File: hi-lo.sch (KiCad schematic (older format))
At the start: 25 parts, among them U31 TC4427, U32 TC4427, U33 TC4427

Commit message: from Ola and Jared (#71)
* Update

* removed fp-info-cache from git

* Gerbers

* moved connector

* Mostly Ola's e-mailed copy, plus some of my own fixes to his almost done revision. I also did some house cleaning, with boundary edges, removed most DRC and ERC errors, etc.

* added Fiducial's
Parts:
- C17, C78: footprint Capacitor_SMD:C_0603_1608Metric_Pad1.05x0.95mm_HandSolder -> Capacitor_SMD:C_0603_1608Metric
- R104, R105, R106, R107, R108, R109, R112, R113, R114, R115, R116, R117, R120, R121, R122, R123, R124, R125, R57, R59: footprint Resistor_SMD:R_0603_1608Metric_Pad1.05x0.95mm_HandSolder -> Resistor_SMD:R_0603_1608Metric
- U31, U32, U33: footprint Package_SO:SO-8_3.9x4.9mm_P1.27mm -> modules:DFN-8-1EP_6x5mm_P1.27mm_EP4x2mm
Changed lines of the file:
@@
 Sheet 3 7
 Title "microRusEfi"
-Date "2019-04-12"
-Rev "0.5.5"
+Date "2019-07-01"
+Rev "R0.2"
 Comp "rusEFI.com"
 Comment1 ""
@@
 F 0 "R125" V 7730 8300 40  0000 C CNN
 F 1 "100" V 7657 8301 40  0000 C CNN
-F 2 "Resistor_SMD:R_0603_1608Metric_Pad1.05x0.95mm_HandSolder" V 980 3050 60  0001 C CNN
+F 2 "Resistor_SMD:R_0603_1608Metric" V 980 3050 60  0001 C CNN
 F 3 "" H 7650 8300 60  0001 C CNN
 	1    7650 8300
@@
 F 0 "R124" V 7730 7700 40  0000 C CNN
 F 1 "100" V 7657 7701 40  0000 C CNN
-F 2 "Resistor_SMD:R_0603_1608Metric_Pad1.05x0.95mm_HandSolder" V 980 3050 60  0001 C CNN
+F 2 "Resistor_SMD:R_0603_1608Metric" V 980 3050 60  0001 C CNN
 F 3 "" H 7650 7700 60  0001 C CNN
 	1    7650 7700
@@
 F 0 "U33" H 6500 8200 60  0000 C CNN
 F 1 "TC4427" H 6650 7700 50  0000 C CNN
-F 2 "Package_SO:SO-8_3.9x4.9mm_P1.27mm" H 6500 7950 60  0001 C CNN
+F 2 "modules:DFN-8-1EP_6x5mm_P1.27mm_EP4x2mm" H 6500 7950 60  0001 C CNN
 F 3 "" H 6500 7950 60  0000 C CNN
 F 4 "579-TC4427EOA" H 0   0   50  0001 C CNN "Part #"
@@
 F 0 "R116" V 5975 8000 40  0000 C CNN
 F 1 "1k" V 5907 8001 40  0000 C CNN
-F 2 "Resistor_SMD:R_0603_1608Metric_Pad1.05x0.95mm_HandSolder" V -770 5150 60  0001 C CNN
+F 2 "Resistor_SMD:R_0603_1608Metric" V -770 5150 60  0001 C CNN
 F 3 "" H 5900 8000 60  0001 C CNN
 	1    5900 8000
@@
 F 0 "R108" V 5475 7900 40  0000 C CNN
 F 1 "20R" V 5407 7901 40  0000 C CNN
-F 2 "Resistor_SMD:R_0603_1608Metric_Pad1.05x0.95mm_HandSolder" V -1270 5050 60  0001 C CNN
+F 2 "Resistor_SMD:R_0603_1608Metric" V -1270 5050 60  0001 C CNN
 F 3 "" H 5400 7900 60  0001 C CNN
 	1    5400 7900
@@
 F 0 "R117" V 5975 8200 40  0000 C CNN
 F 1 "1k" V 5907 8201 40  0000 C CNN
-F 2 "Resistor_SMD:R_0603_1608Metric_Pad1.05x0.95mm_HandSolder" V -770 5350 60  0001 C CNN
+F 2 "Resistor_SMD:R_0603_1608Metric" V -770 5350 60  0001 C CNN
 F 3 "" H 5900 8200 60  0001 C CNN
 	1    5900 8200
@@
 F 0 "R109" V 5475 8100 40  0000 C CNN
 F 1 "20R" V 5407 8101 40  0000 C CNN
-F 2 "Resistor_SMD:R_0603_1608Metric_Pad1.05x0.95mm_HandSolder" V -1270 5250 60  0001 C CNN
+F 2 "Resistor_SMD:R_0603_1608Metric" V -1270 5250 60  0001 C CNN
 F 3 "" H 5400 8100 60  0001 C CNN
 	1    5400 8100
@@
 F 0 "R123" V 7680 7100 40  0000 C CNN
 F 1 "100" V 7607 7101 40  0000 C CNN
-F 2 "Resistor_SMD:R_0603_1608Metric_Pad1.05x0.95mm_HandSolder" V 930 1850 60  0001 C CNN
+F 2 "Resistor_SMD:R_0603_1608Metric" V 930 1850 60  0001 C CNN
 F 3 "" H 7600 7100 60  0001 C CNN
 	1    7600 7100
@@
 F 0 "R122" V 7680 6500 40  0000 C CNN
 F 1 "100" V 7607 6501 40  0000 C CNN
-F 2 "Resistor_SMD:R_0603_1608Metric_Pad1.05x0.95mm_HandSolder" V 930 1850 60  0001 C CNN
+F 2 "Resistor_SMD:R_0603_1608Metric" V 930 1850 60  0001 C CNN
 F 3 "" H 7600 6500 60  0001 C CNN
 	1    7600 6500
@@
 F 0 "U32" H 6450 7000 60  0000 C CNN
 F 1 "TC4427" H 6600 6500 50  0000 C CNN
-F 2 "Package_SO:SO-8_3.9x4.9mm_P1.27mm" H 6450 6750 60  0001 C CNN
+F 2 "modules:DFN-8-1EP_6x5mm_P1.27mm_EP4x2mm" H 6450 6750 60  0001 C CNN
 F 3 "" H 6450 6750 60  0000 C CNN
 F 4 "579-TC4427EOA" H 0   0   50  0001 C CNN "Part #"
@@
 F 0 "R114" V 5925 6800 40  0000 C CNN
 F 1 "1k" V 5857 6801 40  0000 C CNN
-F 2 "Resistor_SMD:R_0603_1608Metric_Pad1.05x0.95mm_HandSolder" V -820 3950 60  0001 C CNN
+F 2 "Resistor_SMD:R_0603_1608Metric" V -820 3950 60  0001 C CNN
 F 3 "" H 5850 6800 60  0001 C CNN
 	1    5850 6800
@@
 F 0 "R106" V 5425 6700 40  0000 C CNN
 F 1 "20R" V 5357 6701 40  0000 C CNN
-F 2 "Resistor_SMD:R_0603_1608Metric_Pad1.05x0.95mm_HandSolder" V -1320 3850 60  0001 C CNN
+F 2 "Resistor_SMD:R_0603_1608Metric" V -1320 3850 60  0001 C CNN
 F 3 "" H 5350 6700 60  0001 C CNN
 	1    5350 6700
@@
 F 0 "R115" V 5925 7000 40  0000 C CNN
 F 1 "1k" V 5857 7001 40  0000 C CNN
-F 2 "Resistor_SMD:R_0603_1608Metric_Pad1.05x0.95mm_HandSolder" V -820 4150 60  0001 C CNN
+F 2 "Resistor_SMD:R_0603_1608Metric" V -820 4150 60  0001 C CNN
 F 3 "" H 5850 7000 60  0001 C CNN
 	1    5850 7000
@@
 F 0 "R107" V 5425 6900 40  0000 C CNN
 F 1 "20R" V 5357 6901 40  0000 C CNN
-F 2 "Resistor_SMD:R_0603_1608Metric_Pad1.05x0.95mm_HandSolder" V -1320 4050 60  0001 C CNN
+F 2 "Resistor_SMD:R_0603_1608Metric" V -1320 4050 60  0001 C CNN
 F 3 "" H 5350 6900 60  0001 C CNN
 	1    5350 6900
@@
 F 0 "C78" V 4250 6850 40  0000 L CNN
 F 1 "10nF" V 4250 6550 40  0000 L CNN
-F 2 "Capacitor_SMD:C_0603_1608Metric_Pad1.05x0.95mm_HandSolder" V -2120 1850 60  0001 C CNN
+F 2 "Capacitor_SMD:C_0603_1608Metric" V -2120 1850 60  0001 C CNN
 F 3 "" H 4200 6800 60  0001 C CNN
 	1    4200 6800
@@
 F 0 "R121" V 7630 5750 40  0000 C CNN
 F 1 "100" V 7557 5751 40  0000 C CNN
-F 2 "Resistor_SMD:R_0603_1608Metric_Pad1.05x0.95mm_HandSolder" V 880 500 60  0001 C CNN
+F 2 "Resistor_SMD:R_0603_1608Metric" V 880 500 60  0001 C CNN
 F 3 "" H 7550 5750 60  0001 C CNN
 	1    7550 5750
@@
 F 0 "R120" V 7630 5150 40  0000 C CNN
 F 1 "100" V 7557 5151 40  0000 C CNN
-F 2 "Resistor_SMD:R_0603_1608Metric_Pad1.05x0.95mm_HandSolder" V 880 500 60  0001 C CNN
+F 2 "Resistor_SMD:R_0603_1608Metric" V 880 500 60  0001 C CNN
 F 3 "" H 7550 5150 60  0001 C CNN
 	1    7550 5150
@@
 F 0 "U31" H 6400 5650 60  0000 C CNN
 F 1 "TC4427" H 6550 5150 50  0000 C CNN
-F 2 "Package_SO:SO-8_3.9x4.9mm_P1.27mm" H 6400 5400 60  0001 C CNN
+F 2 "modules:DFN-8-1EP_6x5mm_P1.27mm_EP4x2mm" H 6400 5400 60  0001 C CNN
 F 3 "" H 6400 5400 60  0000 C CNN
 F 4 "579-TC4427EOA" H 0   0   50  0001 C CNN "Part #"
@@
 F 0 "R112" V 5875 5450 40  0000 C CNN
 F 1 "1k" V 5807 5451 40  0000 C CNN
-F 2 "Resistor_SMD:R_0603_1608Metric_Pad1.05x0.95mm_HandSolder" V -870 2600 60  0001 C CNN
+F 2 "Resistor_SMD:R_0603_1608Metric" V -870 2600 60  0001 C CNN
 F 3 "" H 5800 5450 60  0001 C CNN
 	1    5800 5450
@@
 F 0 "R104" V 5375 5350 40  0000 C CNN
 F 1 "20R" V 5307 5351 40  0000 C CNN
-F 2 "Resistor_SMD:R_0603_1608Metric_Pad1.05x0.95mm_HandSolder" V -1370 2500 60  0001 C CNN
+F 2 "Resistor_SMD:R_0603_1608Metric" V -1370 2500 60  0001 C CNN
 F 3 "" H 5300 5350 60  0001 C CNN
 	1    5300 5350
@@
 F 0 "R113" V 5875 5650 40  0000 C CNN
 F 1 "1k" V 5807 5651 40  0000 C CNN
-F 2 "Resistor_SMD:R_0603_1608Metric_Pad1.05x0.95mm_HandSolder" V -870 2800 60  0001 C CNN
+F 2 "Resistor_SMD:R_0603_1608Metric" V -870 2800 60  0001 C CNN
 F 3 "" H 5800 5650 60  0001 C CNN
 	1    5800 5650
@@
 F 0 "R105" V 5375 5550 40  0000 C CNN
 F 1 "20R" V 5307 5551 40  0000 C CNN
-F 2 "Resistor_SMD:R_0603_1608Metric_Pad1.05x0.95mm_HandSolder" V -1370 2700 60  0001 C CNN
+F 2 "Resistor_SMD:R_0603_1608Metric" V -1370 2700 60  0001 C CNN
 F 3 "" H 5300 5550 60  0001 C CNN
 	1    5300 5550
@@
 F 0 "C17" V 4050 5150 40  0000 L CNN
 F 1 "10nF" V 4050 4850 40  0000 L CNN
-F 2 "Capacitor_SMD:C_0603_1608Metric_Pad1.05x0.95mm_HandSolder" V -2320 150 60  0001 C CNN
+F 2 "Capacitor_SMD:C_0603_1608Metric" V -2320 150 60  0001 C CNN
 F 3 "" H 4000 5100 60  0001 C CNN
 	1    4000 5100
@@
 F 0 "R59" V 3175 5100 40  0000 C CNN
 F 1 "0R" V 3107 5101 40  0000 C CNN
-F 2 "Resistor_SMD:R_0603_1608Metric_Pad1.05x0.95mm_HandSolder" V -3570 2250 60  0001 C CNN
+F 2 "Resistor_SMD:R_0603_1608Metric" V -3570 2250 60  0001 C CNN
 F 3 "" H 3100 5100 60  0001 C CNN
 	1    3100 5100
@@
 F 0 "R57" V 3175 4800 40  0000 C CNN
 F 1 "DNP" V 3107 4801 40  0000 C CNN
-F 2 "Resistor_SMD:R_0603_1608Metric_Pad1.05x0.95mm_HandSolder" V -3570 1950 60  0001 C CNN
+F 2 "Resistor_SMD:R_0603_1608Metric" V -3570 1950 60  0001 C CNN
 F 3 "" H 3100 4800 60  0001 C CNN
 	1    3100 4800

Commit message: Updated logo symbol and footprint, BOM is 99% entered in KC schematic now.
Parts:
- C17, C78: Manufacturer (none) -> KEMET; Part # (none) -> C0603C103K1RACTU; VEND (none) -> DIGI; VEND# (none) -> 399-3189-1-ND
- R104, R105, R106, R107, R108, R109: Manufacturer (none) -> StackPole; Part # (none) -> RMCF0603JT20R0; VEND (none) -> DIGI; VEND# (none) -> RMCF0603JT20R0CT-ND
- R112, R113, R114, R115, R116, R117: Manufacturer (none) -> StackPole; Part # (none) -> RMCF0603JJ1K00; VEND (none) -> DIGI; VEND# (none) -> RMCF0603JJ1K00CT-ND
- R120, R121, R122, R123, R124, R125: Manufacturer (none) -> StackPole; Part # (none) -> RMCF0603FT100R; VEND (none) -> DIGI; VEND# (none) -> RMCF0603FT100RCT-ND
- R57: Manufacturer (none) -> DNP; Part # (none) -> DNP; VEND (none) -> DIGI; VEND# (none) -> DNP
- R59: Manufacturer (none) -> StackPole; Part # (none) -> RMCF0603ZT0R00; VEND (none) -> DIGI; VEND# (none) -> RMCF0603ZT0R00CT-ND
- U31, U32, U33: Manufacturer (none) -> MicroChip; Part # 579-TC4427EOA -> TC4427EOA; VEND (none) -> DIGI; VEND# 579-TC4427EOA -> TC4427EOA-ND
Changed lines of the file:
@@
 F 2 "Resistor_SMD:R_0603_1608Metric" V 980 3050 60  0001 C CNN
 F 3 "" H 7650 8300 60  0001 C CNN
+F 4 "RMCF0603FT100R" H 0   0   50  0001 C CNN "Part #"
+F 5 "DIGI" H 0   0   50  0001 C CNN "VEND"
+F 6 "RMCF0603FT100RCT-ND" H 0   0   50  0001 C CNN "VEND#"
+F 7 "StackPole" H 0   0   50  0001 C CNN "Manufacturer"
 	1    7650 8300
 	0    1    1    0
@@
 F 2 "Resistor_SMD:R_0603_1608Metric" V 980 3050 60  0001 C CNN
 F 3 "" H 7650 7700 60  0001 C CNN
+F 4 "RMCF0603FT100R" H 0   0   50  0001 C CNN "Part #"
+F 5 "DIGI" H 0   0   50  0001 C CNN "VEND"
+F 6 "RMCF0603FT100RCT-ND" H 0   0   50  0001 C CNN "VEND#"
+F 7 "StackPole" H 0   0   50  0001 C CNN "Manufacturer"
 	1    7650 7700
 	0    1    -1   0
@@
 F 2 "modules:DFN-8-1EP_6x5mm_P1.27mm_EP4x2mm" H 6500 7950 60  0001 C CNN
 F 3 "" H 6500 7950 60  0000 C CNN
-F 4 "579-TC4427EOA" H 0   0   50  0001 C CNN "Part #"
-F 5 "579-TC4427EOA" H 0   0   50  0001 C CNN "VEND#"
+F 4 "TC4427EOA" H 0   0   50  0001 C CNN "Part #"
+F 5 "TC4427EOA-ND" H 0   0   50  0001 C CNN "VEND#"
+F 6 "DIGI" H 0   0   50  0001 C CNN "VEND"
+F 7 "MicroChip" H 0   0   50  0001 C CNN "Manufacturer"
 	1    6500 7950
 	1    0    0    -1
@@
 F 2 "Resistor_SMD:R_0603_1608Metric" V -770 5150 60  0001 C CNN
 F 3 "" H 5900 8000 60  0001 C CNN
+F 4 "RMCF0603JJ1K00" H 0   0   50  0001 C CNN "Part #"
+F 5 "DIGI" H 0   0   50  0001 C CNN "VEND"
+F 6 "RMCF0603JJ1K00CT-ND" H 0   0   50  0001 C CNN "VEND#"
+F 7 "StackPole" H 0   0   50  0001 C CNN "Manufacturer"
 	1    5900 8000
 	0    1    -1   0
@@
 F 2 "Resistor_SMD:R_0603_1608Metric" V -1270 5050 60  0001 C CNN
 F 3 "" H 5400 7900 60  0001 C CNN
+F 4 "RMCF0603JT20R0" H 0   0   50  0001 C CNN "Part #"
+F 5 "DIGI" H 0   0   50  0001 C CNN "VEND"
+F 6 "RMCF0603JT20R0CT-ND" H 0   0   50  0001 C CNN "VEND#"
+F 7 "StackPole" H 0   0   50  0001 C CNN "Manufacturer"
 	1    5400 7900
 	0    1    -1   0
@@
 F 2 "Resistor_SMD:R_0603_1608Metric" V -770 5350 60  0001 C CNN
 F 3 "" H 5900 8200 60  0001 C CNN
+F 4 "RMCF0603JJ1K00" H 0   0   50  0001 C CNN "Part #"
+F 5 "DIGI" H 0   0   50  0001 C CNN "VEND"
+F 6 "RMCF0603JJ1K00CT-ND" H 0   0   50  0001 C CNN "VEND#"
+F 7 "StackPole" H 0   0   50  0001 C CNN "Manufacturer"
 	1    5900 8200
 	0    1    -1   0
@@
 F 2 "Resistor_SMD:R_0603_1608Metric" V -1270 5250 60  0001 C CNN
 F 3 "" H 5400 8100 60  0001 C CNN
+F 4 "RMCF0603JT20R0" H 0   0   50  0001 C CNN "Part #"
+F 5 "DIGI" H 0   0   50  0001 C CNN "VEND"
+F 6 "RMCF0603JT20R0CT-ND" H 0   0   50  0001 C CNN "VEND#"
+F 7 "StackPole" H 0   0   50  0001 C CNN "Manufacturer"
 	1    5400 8100
 	0    1    -1   0
@@
 F 2 "Resistor_SMD:R_0603_1608Metric" V 930 1850 60  0001 C CNN
 F 3 "" H 7600 7100 60  0001 C CNN
+F 4 "RMCF0603FT100R" H 0   0   50  0001 C CNN "Part #"
+F 5 "DIGI" H 0   0   50  0001 C CNN "VEND"
+F 6 "RMCF0603FT100RCT-ND" H 0   0   50  0001 C CNN "VEND#"
+F 7 "StackPole" H 0   0   50  0001 C CNN "Manufacturer"
 	1    7600 7100
 	0    1    1    0
@@
 F 2 "Resistor_SMD:R_0603_1608Metric" V 930 1850 60  0001 C CNN
 F 3 "" H 7600 6500 60  0001 C CNN
+F 4 "RMCF0603FT100R" H 0   0   50  0001 C CNN "Part #"
+F 5 "DIGI" H 0   0   50  0001 C CNN "VEND"
+F 6 "RMCF0603FT100RCT-ND" H 0   0   50  0001 C CNN "VEND#"
+F 7 "StackPole" H 0   0   50  0001 C CNN "Manufacturer"
 	1    7600 6500
 	0    1    -1   0
@@
 F 2 "modules:DFN-8-1EP_6x5mm_P1.27mm_EP4x2mm" H 6450 6750 60  0001 C CNN
 F 3 "" H 6450 6750 60  0000 C CNN
-F 4 "579-TC4427EOA" H 0   0   50  0001 C CNN "Part #"
-F 5 "579-TC4427EOA" H 0   0   50  0001 C CNN "VEND#"
+F 4 "TC4427EOA" H 0   0   50  0001 C CNN "Part #"
+F 5 "TC4427EOA-ND" H 0   0   50  0001 C CNN "VEND#"
+F 6 "DIGI" H 0   0   50  0001 C CNN "VEND"
+F 7 "MicroChip" H 0   0   50  0001 C CNN "Manufacturer"
 	1    6450 6750
 	1    0    0    -1
@@
 F 2 "Resistor_SMD:R_0603_1608Metric" V -820 3950 60  0001 C CNN
 F 3 "" H 5850 6800 60  0001 C CNN
+F 4 "RMCF0603JJ1K00" H 0   0   50  0001 C CNN "Part #"
+F 5 "DIGI" H 0   0   50  0001 C CNN "VEND"
+F 6 "RMCF0603JJ1K00CT-ND" H 0   0   50  0001 C CNN "VEND#"
+F 7 "StackPole" H 0   0   50  0001 C CNN "Manufacturer"
 	1    5850 6800
 	0    1    -1   0
@@
 F 2 "Resistor_SMD:R_0603_1608Metric" V -1320 3850 60  0001 C CNN
 F 3 "" H 5350 6700 60  0001 C CNN
+F 4 "RMCF0603JT20R0" H 0   0   50  0001 C CNN "Part #"
+F 5 "DIGI" H 0   0   50  0001 C CNN "VEND"
+F 6 "RMCF0603JT20R0CT-ND" H 0   0   50  0001 C CNN "VEND#"
+F 7 "StackPole" H 0   0   50  0001 C CNN "Manufacturer"
 	1    5350 6700
 	0    1    -1   0
@@
 F 2 "Resistor_SMD:R_0603_1608Metric" V -820 4150 60  0001 C CNN
 F 3 "" H 5850 7000 60  0001 C CNN
+F 4 "RMCF0603JJ1K00" H 0   0   50  0001 C CNN "Part #"
+F 5 "DIGI" H 0   0   50  0001 C CNN "VEND"
+F 6 "RMCF0603JJ1K00CT-ND" H 0   0   50  0001 C CNN "VEND#"
+F 7 "StackPole" H 0   0   50  0001 C CNN "Manufacturer"
 	1    5850 7000
 	0    1    -1   0
@@
 F 2 "Resistor_SMD:R_0603_1608Metric" V -1320 4050 60  0001 C CNN
 F 3 "" H 5350 6900 60  0001 C CNN
+F 4 "RMCF0603JT20R0" H 0   0   50  0001 C CNN "Part #"
+F 5 "DIGI" H 0   0   50  0001 C CNN "VEND"
+F 6 "RMCF0603JT20R0CT-ND" H 0   0   50  0001 C CNN "VEND#"
+F 7 "StackPole" H 0   0   50  0001 C CNN "Manufacturer"
 	1    5350 6900
 	0    1    -1   0
@@
 F 2 "Capacitor_SMD:C_0603_1608Metric" V -2120 1850 60  0001 C CNN
 F 3 "" H 4200 6800 60  0001 C CNN
+F 4 "C0603C103K1RACTU" H 0   0   50  0001 C CNN "Part #"
+F 5 "DIGI" H 0   0   50  0001 C CNN "VEND"
+F 6 "399-3189-1-ND" H 0   0   50  0001 C CNN "VEND#"
+F 7 "KEMET" H 0   0   50  0001 C CNN "Manufacturer"
 	1    4200 6800
 	0    1    -1   0
@@
 F 2 "Resistor_SMD:R_0603_1608Metric" V 880 500 60  0001 C CNN
 F 3 "" H 7550 5750 60  0001 C CNN
+F 4 "RMCF0603FT100R" H 0   0   50  0001 C CNN "Part #"
+F 5 "DIGI" H 0   0   50  0001 C CNN "VEND"
+F 6 "RMCF0603FT100RCT-ND" H 0   0   50  0001 C CNN "VEND#"
+F 7 "StackPole" H 0   0   50  0001 C CNN "Manufacturer"
 	1    7550 5750
 	0    1    1    0
@@
 F 2 "Resistor_SMD:R_0603_1608Metric" V 880 500 60  0001 C CNN
 F 3 "" H 7550 5150 60  0001 C CNN
+F 4 "RMCF0603FT100R" H 0   0   50  0001 C CNN "Part #"
+F 5 "DIGI" H 0   0   50  0001 C CNN "VEND"
+F 6 "RMCF0603FT100RCT-ND" H 0   0   50  0001 C CNN "VEND#"
+F 7 "StackPole" H 0   0   50  0001 C CNN "Manufacturer"
 	1    7550 5150
 	0    1    -1   0
@@
 F 2 "modules:DFN-8-1EP_6x5mm_P1.27mm_EP4x2mm" H 6400 5400 60  0001 C CNN
 F 3 "" H 6400 5400 60  0000 C CNN
-F 4 "579-TC4427EOA" H 0   0   50  0001 C CNN "Part #"
-F 5 "579-TC4427EOA" H 0   0   50  0001 C CNN "VEND#"
+F 4 "TC4427EOA" H 0   0   50  0001 C CNN "Part #"
+F 5 "TC4427EOA-ND" H 0   0   50  0001 C CNN "VEND#"
+F 6 "DIGI" H 0   0   50  0001 C CNN "VEND"
+F 7 "MicroChip" H 0   0   50  0001 C CNN "Manufacturer"
 	1    6400 5400
 	1    0    0    -1
@@
 F 2 "Resistor_SMD:R_0603_1608Metric" V -870 2600 60  0001 C CNN
 F 3 "" H 5800 5450 60  0001 C CNN
+F 4 "RMCF0603JJ1K00" H 0   0   50  0001 C CNN "Part #"
+F 5 "DIGI" H 0   0   50  0001 C CNN "VEND"
+F 6 "RMCF0603JJ1K00CT-ND" H 0   0   50  0001 C CNN "VEND#"
+F 7 "StackPole" H 0   0   50  0001 C CNN "Manufacturer"
 	1    5800 5450
 	0    1    -1   0
@@
 F 2 "Resistor_SMD:R_0603_1608Metric" V -1370 2500 60  0001 C CNN
 F 3 "" H 5300 5350 60  0001 C CNN
+F 4 "RMCF0603JT20R0" H 0   0   50  0001 C CNN "Part #"
+F 5 "DIGI" H 0   0   50  0001 C CNN "VEND"
+F 6 "RMCF0603JT20R0CT-ND" H 0   0   50  0001 C CNN "VEND#"
+F 7 "StackPole" H 0   0   50  0001 C CNN "Manufacturer"
 	1    5300 5350
 	0    1    -1   0
@@
 F 2 "Resistor_SMD:R_0603_1608Metric" V -870 2800 60  0001 C CNN
 F 3 "" H 5800 5650 60  0001 C CNN
+F 4 "RMCF0603JJ1K00" H 0   0   50  0001 C CNN "Part #"
+F 5 "DIGI" H 0   0   50  0001 C CNN "VEND"
+F 6 "RMCF0603JJ1K00CT-ND" H 0   0   50  0001 C CNN "VEND#"
+F 7 "StackPole" H 0   0   50  0001 C CNN "Manufacturer"
 	1    5800 5650
 	0    1    -1   0
@@
 F 2 "Resistor_SMD:R_0603_1608Metric" V -1370 2700 60  0001 C CNN
 F 3 "" H 5300 5550 60  0001 C CNN
+F 4 "RMCF0603JT20R0" H 0   0   50  0001 C CNN "Part #"
+F 5 "DIGI" H 0   0   50  0001 C CNN "VEND"
+F 6 "RMCF0603JT20R0CT-ND" H 0   0   50  0001 C CNN "VEND#"
+F 7 "StackPole" H 0   0   50  0001 C CNN "Manufacturer"
 	1    5300 5550
 	0    1    -1   0
@@
 F 2 "Capacitor_SMD:C_0603_1608Metric" V -2320 150 60  0001 C CNN
 F 3 "" H 4000 5100 60  0001 C CNN
+F 4 "C0603C103K1RACTU" H 0   0   50  0001 C CNN "Part #"
+F 5 "DIGI" H 0   0   50  0001 C CNN "VEND"
+F 6 "399-3189-1-ND" H 0   0   50  0001 C CNN "VEND#"
+F 7 "KEMET" H 0   0   50  0001 C CNN "Manufacturer"
 	1    4000 5100
 	-1   0    0    -1
@@
 F 2 "Resistor_SMD:R_0603_1608Metric" V -3570 2250 60  0001 C CNN
 F 3 "" H 3100 5100 60  0001 C CNN
+F 4 "RMCF0603ZT0R00" H 0   0   50  0001 C CNN "Part #"
+F 5 "DIGI" H 0   0   50  0001 C CNN "VEND"
+F 6 "RMCF0603ZT0R00CT-ND" H 0   0   50  0001 C CNN "VEND#"
+F 7 "StackPole" H 0   0   50  0001 C CNN "Manufacturer"
 	1    3100 5100
 	1    0    0    1
@@
 F 2 "Resistor_SMD:R_0603_1608Metric" V -3570 1950 60  0001 C CNN
 F 3 "" H 3100 4800 60  0001 C CNN
+F 4 "DNP" H 0   0   50  0001 C CNN "Part #"
+F 5 "DIGI" H 0   0   50  0001 C CNN "VEND"
+F 6 "DNP" H 0   0   50  0001 C CNN "VEND#"
+F 7 "DNP" H 0   0   50  0001 C CNN "Manufacturer"
 	1    3100 4800
 	1    0    0    1

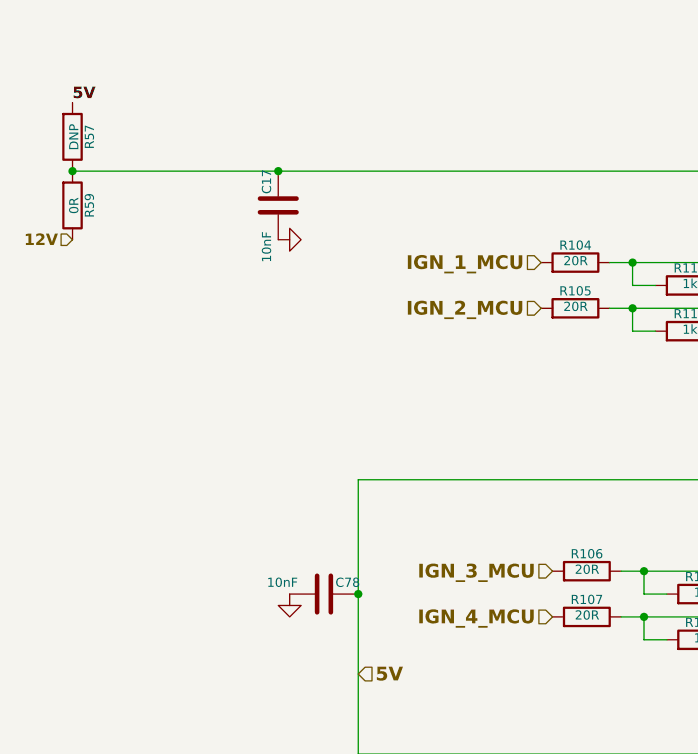
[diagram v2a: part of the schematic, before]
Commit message: sync (#98)
* Added silk screen mark, minor schematic formatting.
https://github.com/rusefi/hw_microRusEfi/issues/89

* Changed SWD connector to reflect validated brain board.
https://github.com/rusefi/hw_microRusEfi/issues/88

* Changed R26 into push button SW1 BOM is still TBD
https://github.com/rusefi/hw_microRusEfi/issues/86

* coil1 silk was corrected to coil2
https://github.com/rusefi/hw_microRusEfi/issues/90

* Updated BOM
https://github.com/rusefi/hw_microRusEfi/issues/94
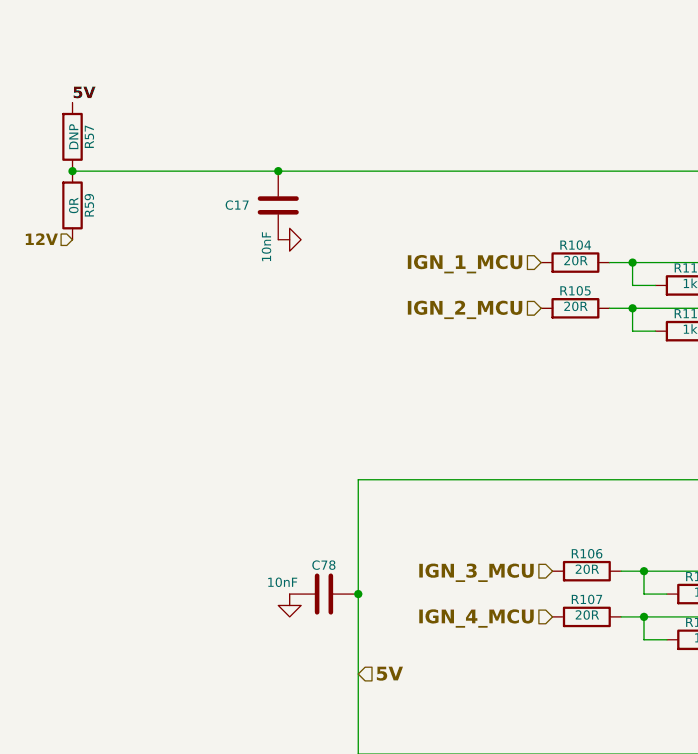
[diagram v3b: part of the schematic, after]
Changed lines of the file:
@@
 U 1 1 5D15752C
 P 4200 6800
-F 0 "C78" V 4250 6850 40  0000 L CNN
+F 0 "C78" V 4325 6800 40  0000 C CNN
 F 1 "10nF" V 4250 6550 40  0000 L CNN
 F 2 "Capacitor_SMD:C_0603_1608Metric" V -2120 1850 60  0001 C CNN
@@
 U 1 1 5E89211D
 P 4000 5100
-F 0 "C17" V 4050 5150 40  0000 L CNN
+F 0 "C17" H 4125 5100 40  0000 L CNN
 F 1 "10nF" V 4050 4850 40  0000 L CNN
 F 2 "Capacitor_SMD:C_0603_1608Metric" V -2320 150 60  0001 C CNN

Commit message: getting closer to 0.3
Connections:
- net HS1 renamed Ign3
- net HS1_MCU renamed Ign3_MCU
- net HS2 renamed Ign4
- net HS2_MCU renamed Ign4_MCU
- net IGN_1 renamed GP5
- net IGN_1_MCU renamed GP5_MCU
- net IGN_2 renamed GP6
- net IGN_2_MCU renamed GP6_MCU
- net IGN_3 renamed Ign1
- net IGN_3_MCU renamed Ign1_MCU
- net IGN_4 renamed Ign2
- net IGN_4_MCU renamed Ign2_MCU
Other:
- note added: "6 channel high / low side driver"
- note removed: "8 channel high / low side driver"
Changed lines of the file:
@@
 $EndDescr
 Text Notes 6250 3300 0    160  ~ 32
-8 channel high / low side driver
+6 channel high / low side driver
 NoConn ~ 6150 7800
 NoConn ~ 6850 7800
@@
 	6850 4950 6850 5450
 Text HLabel 7700 5150 2    60   Input ~ 12
-IGN_1
+GP5
 Text HLabel 7700 5750 2    60   Input ~ 12
-IGN_2
+GP6
 Text HLabel 7750 6500 2    60   Input ~ 12
-IGN_3
+Ign1
 Text HLabel 7750 7100 2    60   Input ~ 12
-IGN_4
+Ign2
 Text HLabel 7800 7700 2    60   Input ~ 12
-HS1
+Ign3
 Text HLabel 7800 8300 2    60   Input ~ 12
-HS2
+Ign4
 Text HLabel 5150 5350 0    60   Input ~ 12
-IGN_1_MCU
+GP5_MCU
 Text HLabel 5150 5550 0    60   Input ~ 12
-IGN_2_MCU
+GP6_MCU
 Text HLabel 5200 6700 0    60   Input ~ 12
-IGN_3_MCU
+Ign1_MCU
 Text HLabel 5200 6900 0    60   Input ~ 12
-IGN_4_MCU
+Ign2_MCU
 Text HLabel 5250 7900 0    60   Input ~ 12
-HS1_MCU
+Ign3_MCU
 Text HLabel 5250 8100 0    60   Input ~ 12
-HS2_MCU
+Ign4_MCU
 Wire Wire Line
 	4350 6300 4350 6800
